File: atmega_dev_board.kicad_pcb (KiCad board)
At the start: 4 copper layers, 26.8 x 53 mm, 39 parts, among them J1 1x15 Pin Header, J2 USB_C_Receptacle_USB2.0_16P, J3 1x15 Pin Header, J4 ICSP Header, SW1 Push button switch, SW2 Push button switch, U1 L78L05_SOT89, U2 L78L33_SOT89, U3 ATmega328P-A, U4 CP2102N-Axx-xQFN28, Y1 Crystal 16MHz

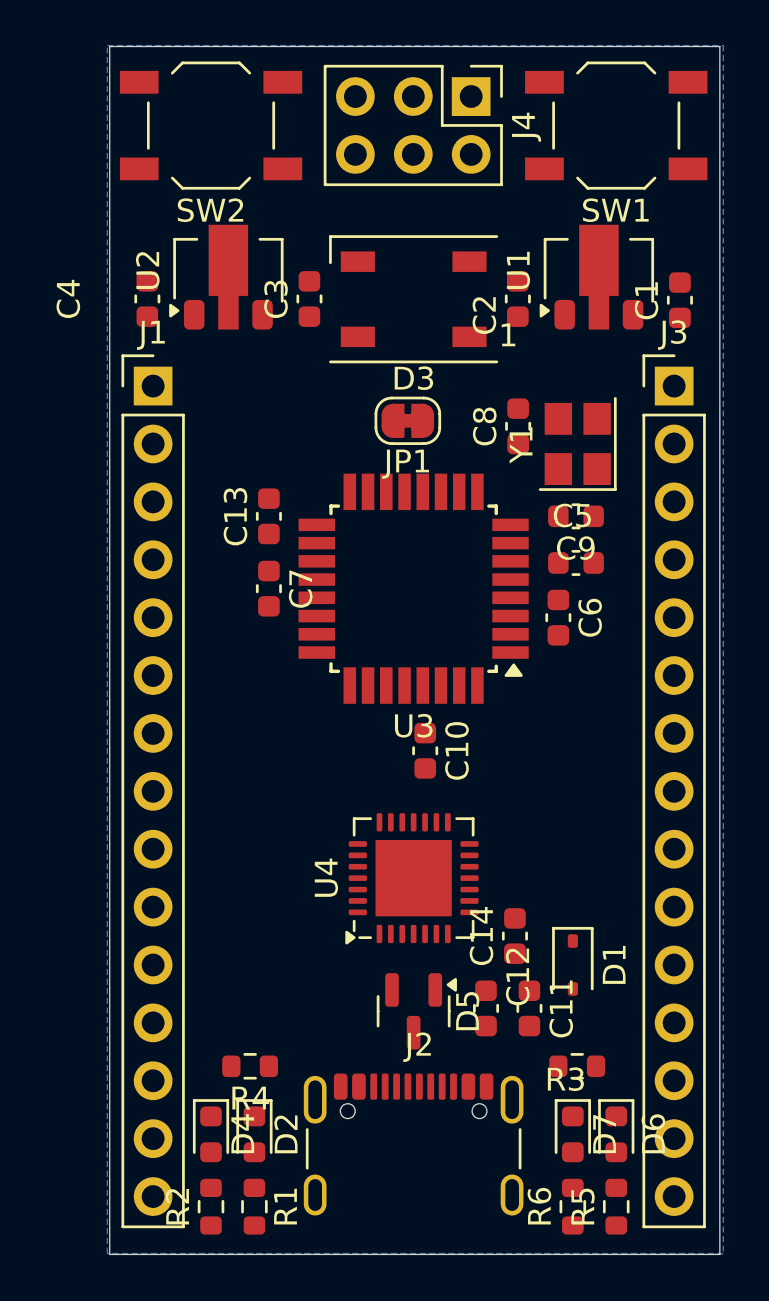
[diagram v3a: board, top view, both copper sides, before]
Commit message: Tidy up schema and route all but GPIO traces
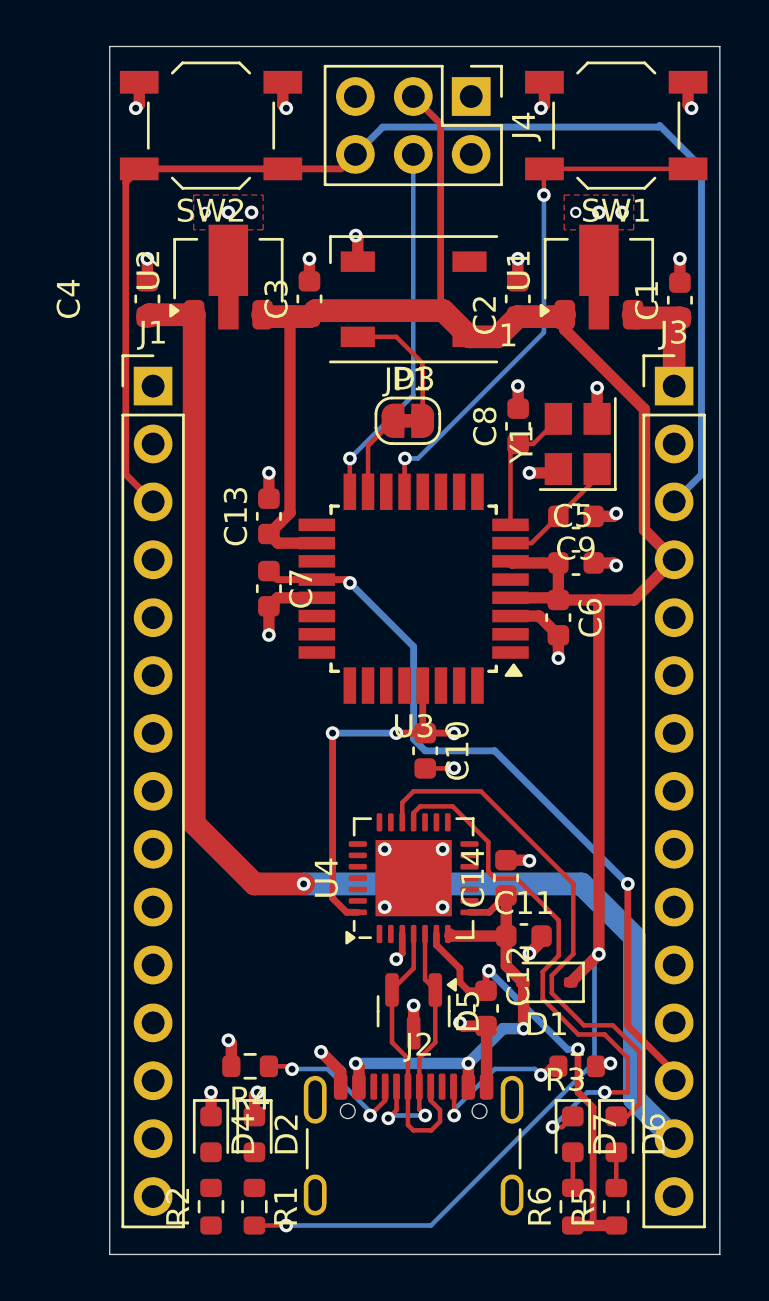
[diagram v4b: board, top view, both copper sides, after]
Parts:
- moved C11 3.18 mm to (222.0, 118.1), turned to 0 degrees
- moved C14 2.58 mm to (221.2, 115.6)
- moved D1 1.37 mm to (223.0, 120.1), turned to 180 degrees
- turned JP1 to 0 degrees
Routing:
- net +5V: track 0.00 -> 100.9 mm, vias 0 -> 2
- net /RESET: track 0.00 -> 72.8 mm, vias 0 -> 3
- net +3V3: track 0.00 -> 55.4 mm, vias 0 -> 1
- net GND: track 0.00 -> 41.2 mm, vias 0 -> 38
- net /AREF: track 0.00 -> 33.3 mm, vias 0 -> 2
- net /RXT: track 0.00 -> 24.8 mm, vias 0 -> 2
- net /TXT: track 0.00 -> 23.9 mm
- net /D9: track 0.00 -> 23.3 mm, vias 0 -> 2
- net VBUS: track 0.00 -> 20.7 mm, vias 0 -> 3
- net /CP_VDD: track 0.00 -> 20.0 mm, vias 0 -> 2
- net /D12: track 0.00 -> 16.0 mm, vias 0 -> 1
- net /USB_D+: track 0.00 -> 12.4 mm
- net /USB_D-: track 0.00 -> 11.8 mm, vias 0 -> 2
- net /USB_CC2: track 0.00 -> 7.11 mm, vias 0 -> 2
- net /USB_CC1: track 0.00 -> 6.98 mm, vias 0 -> 2
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- added copper zone on F.Cu, net GND
- removed copper zone on B.Cu, net GND

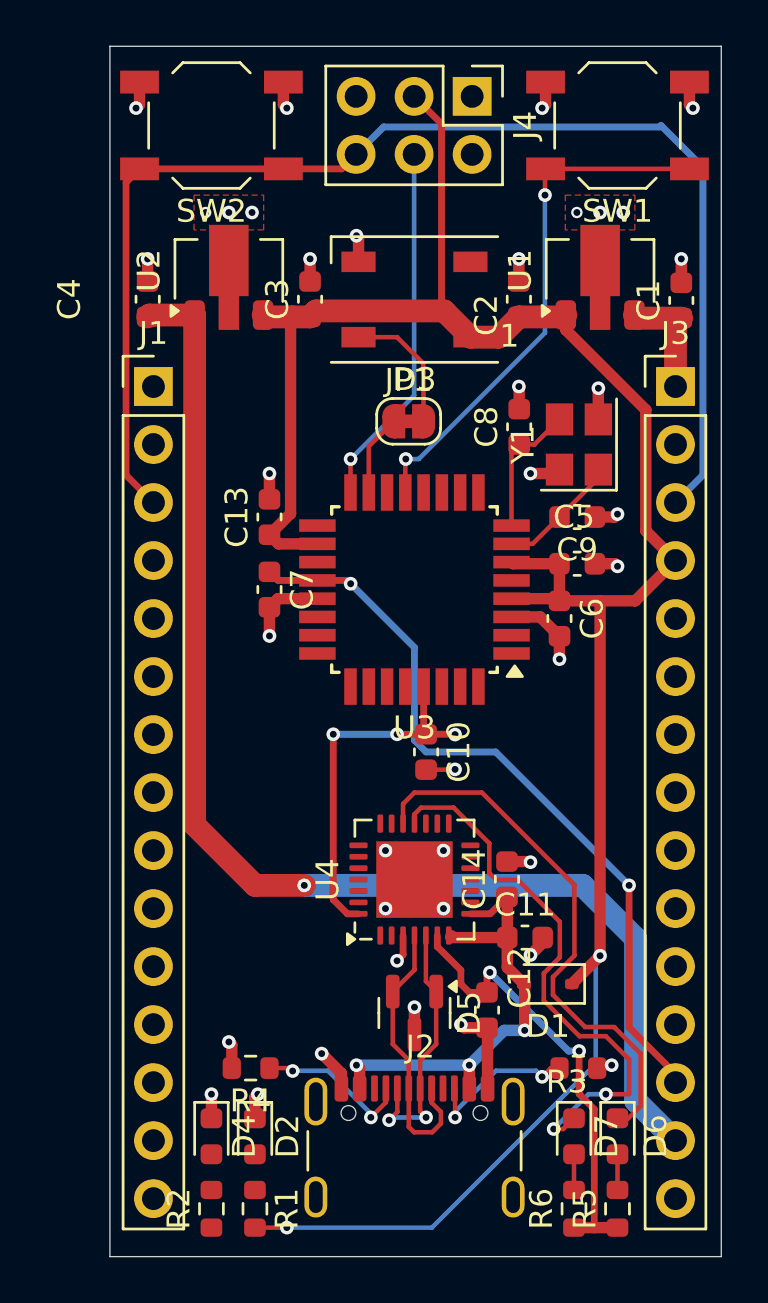
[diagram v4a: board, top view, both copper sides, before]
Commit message: Update PCB meta data. More GPIO routing
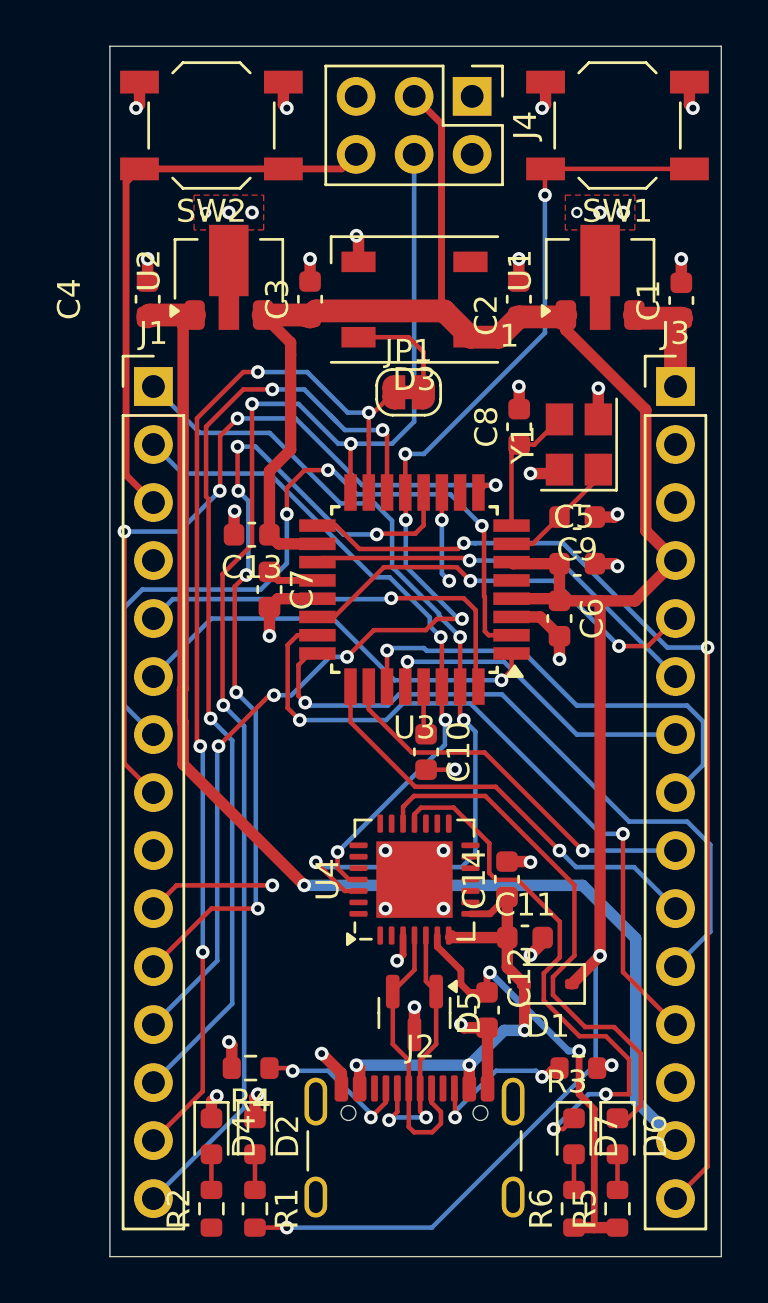
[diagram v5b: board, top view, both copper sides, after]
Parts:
- D1: value Diode Schottky -> 1N5819WS
- D2, D4, D6, D7: value LED -> RED
- D5: value SM712_SOT23 -> PSM712
- J2: value USB_C_Receptacle_USB2.0_16P -> U263-163N-4BLS1735
- J4: value ICSP Header -> 2x3 Pin Header
- SW1, SW2: value Push button switch -> Push Button
- U1: value L78L05_SOT89 -> 78L05G-AB3-R
- U2: value L78L33_SOT89 -> HT7533-1
- Y1: value Crystal 16MHz -> 16 MHz
- moved JP1 1.27 mm to (216.9, 94.2)
- moved C13 1.10 mm to (210.0, 100.5), turned to 180 degrees
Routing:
- net /RESET: track 72.8 -> 27.2 mm, vias 3 -> 0
- net /D13: track 0.00 -> 44.2 mm, vias 0 -> 2
- net /D12: track 16.0 -> 59.4 mm, vias 1 -> 3
- net /D11: track 3.57 -> 46.7 mm, vias 0 -> 4
- net /D10: track 0.00 -> 42.9 mm, vias 0 -> 3
- net /D1: track 0.00 -> 38.7 mm, vias 0 -> 3
- net /D8: track 0.00 -> 38.1 mm, vias 0 -> 6
- net /D5: track 0.00 -> 33.8 mm, vias 0 -> 4
- net /D9: track 23.3 -> 56.5 mm, vias 2 -> 7
- net /D4: track 0.00 -> 33.1 mm, vias 0 -> 3
- net /A0: track 0.00 -> 31.1 mm, vias 0 -> 2
- net /AREF: track 33.3 -> 2.26 mm, vias 2 -> 0
- net /D0: track 0.00 -> 29.6 mm, vias 0 -> 3
- net /A1: track 0.00 -> 29.5 mm, vias 0 -> 1
- net /A4: track 0.00 -> 20.4 mm, vias 0 -> 1
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
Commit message: Finish routing, update design rules
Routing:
- net /RESET: track 27.2 -> 97.4 mm, vias 0 -> 8
- net /D13: track 44.2 -> 107.2 mm
- net /D6: track 0.00 -> 51.6 mm, vias 0 -> 5
- net /AREF: track 2.26 -> 43.9 mm, vias 0 -> 7
- net /D7: track 9.63 -> 31.2 mm, vias 3 -> 6
- net /D11: track 46.7 -> 63.9 mm
- net /D1: track 38.7 -> 45.1 mm
- net +5V: track 101.4 -> 106.0 mm
- net GND: track 41.1 -> 44.9 mm
- net /D0: track 29.6 -> 33.1 mm
- net /A1: track 29.5 -> 27.6 mm
- net /A7: track 18.5 -> 20.4 mm
- net /A0: track 31.1 -> 32.8 mm
- net /D3: track 18.8 -> 17.7 mm
- net /A2: track 19.2 -> 20.1 mm
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
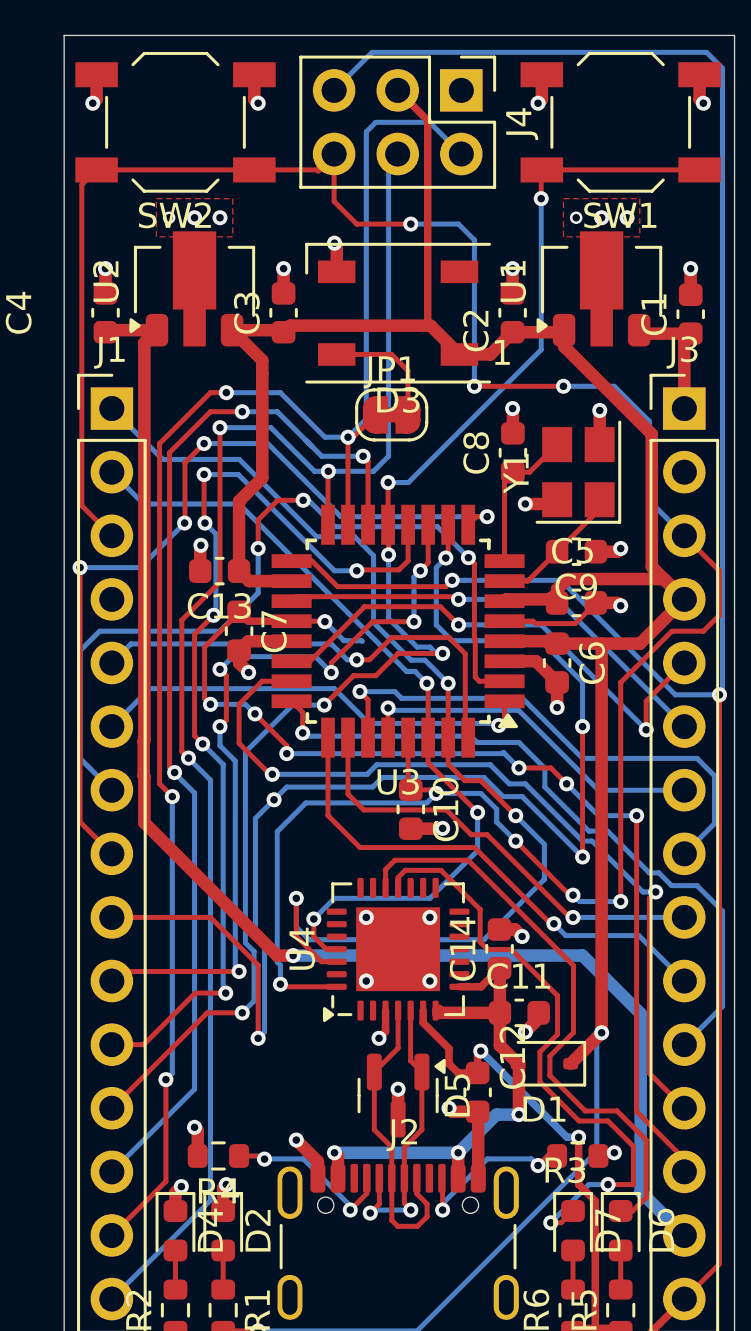
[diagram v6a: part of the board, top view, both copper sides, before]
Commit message: Swap out TVS diodes. Ground USB shield
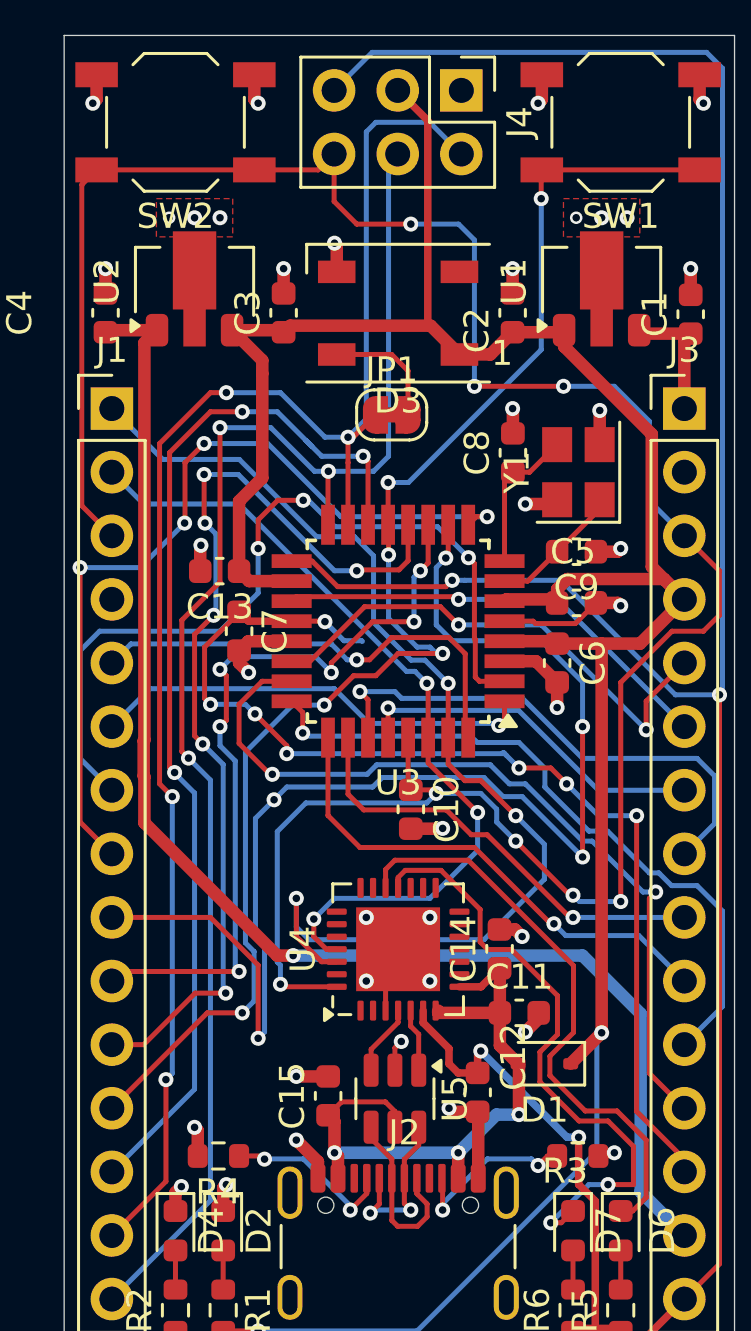
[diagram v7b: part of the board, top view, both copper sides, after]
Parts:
- removed D5: PSM712, Package_TO_SOT_SMD:SOT-23
- added C15: 100n, Capacitor_SMD:C_0603_1608Metric, F.Cu at (214.4, 121.4)
- added U5: USBLC6-2SC6, Package_TO_SOT_SMD:SOT-23-6, F.Cu at (217.0, 121.5)
- C8, C9: value 22p -> 12p
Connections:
- J2 pad A6: /USB_D+ -> /CONN_USB_D+
- J2 pad A7: /USB_D- -> /CONN_USB_D-
- J2 pad B6: /USB_D+ -> /CONN_USB_D+
- J2 pad B7: /USB_D- -> /CONN_USB_D-
- J2 pad S1: unconnected-(J2-SHIELD-PadS1)_1 -> GND
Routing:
- net /USB_D+: track 12.4 -> 2.83 mm
- net /USB_D-: track 11.8 -> 2.52 mm, vias 2 -> 0
- net /CONN_USB_D+: track 0.00 -> 7.43 mm
- net /CONN_USB_D-: track 0.00 -> 6.86 mm, vias 0 -> 2
- net VBUS: track 20.7 -> 26.0 mm
- net GND: track 44.9 -> 47.7 mm
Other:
- rule pad_to_mask_clearance: 0 -> 0.038
- rule solder_mask_min_width: 0.08 -> 0.1

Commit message: Update BOM and component values
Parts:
- J2: value U263-163N-4BLS1735 -> USB_C_Receptacle_USB2.0_16P
